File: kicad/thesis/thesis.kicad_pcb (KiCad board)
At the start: 2 copper layers, 100 x 75 mm, 22 parts, among them J1 Conn_01x01_Socket, J2 Conn_01x01_Socket, J3 Conn_01x07_Socket, J4 Conn_01x04_Socket, Q1 IRLZB8721, U1 INA219AxD

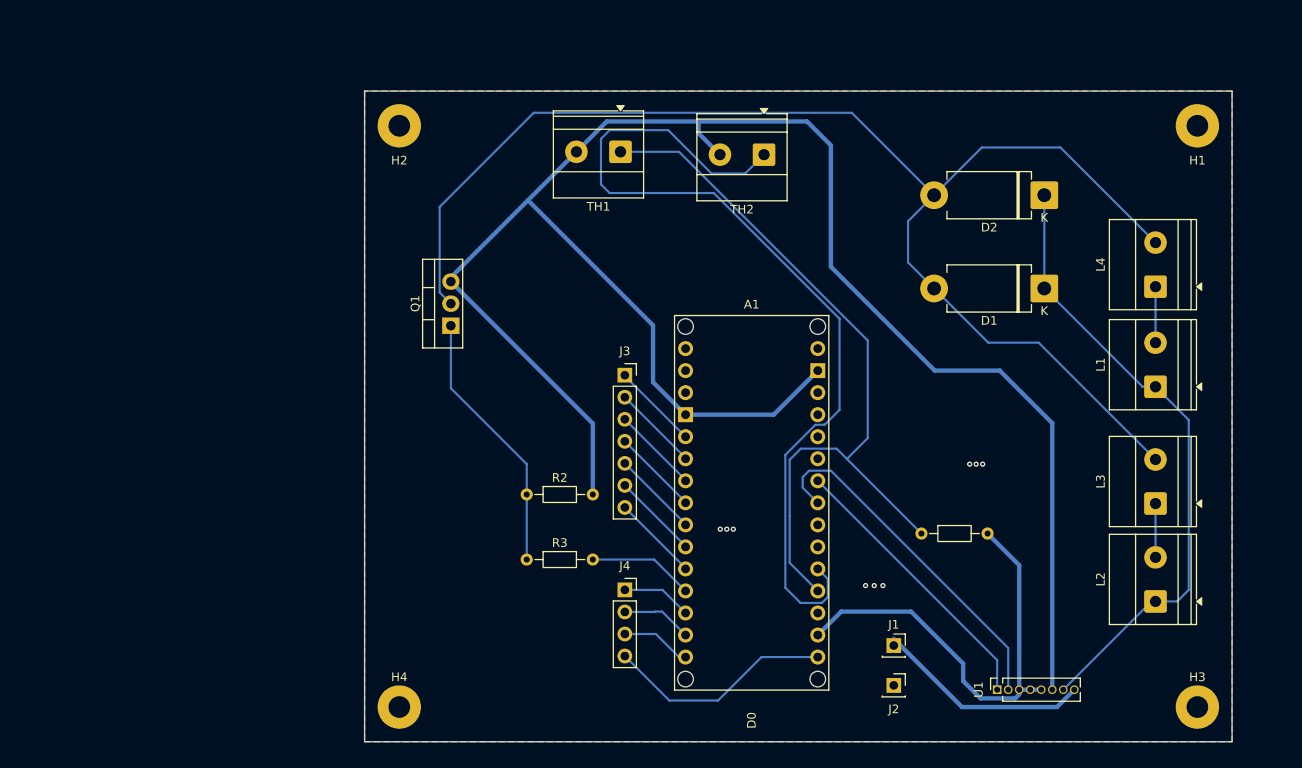
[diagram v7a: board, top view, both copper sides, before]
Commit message: Added pin sockets, header expansion, fixed INA and RC circuit
Need more labels but for now ok ra
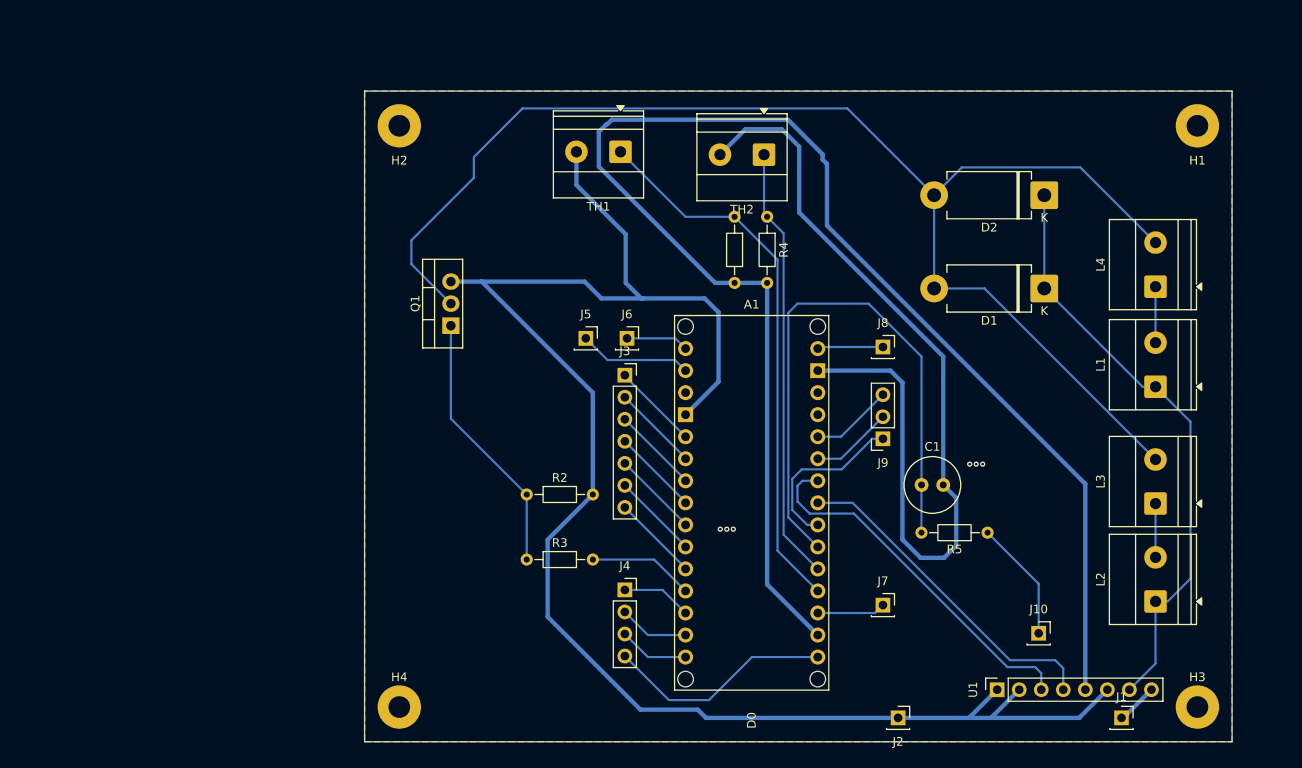
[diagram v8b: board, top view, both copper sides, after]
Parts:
- added C1: 100uF, Capacitor_THT:C_Radial_D6.3mm_H7.0mm_P2.50mm, F.Cu at (158.2, 104.4)
- added J10: Conn_01x01_Socket, Connector_PinSocket_2.54mm:PinSocket_1x01_P2.54mm_Vertical, F.Cu at (171.7, 121.5)
- added J5: Conn_01x01_Socket, Connector_PinSocket_2.54mm:PinSocket_1x01_P2.54mm_Vertical, F.Cu at (119.5, 87.5)
- added J6: Conn_01x01_Socket, Connector_PinSocket_2.54mm:PinSocket_1x01_P2.54mm_Vertical, F.Cu at (124.2, 87.5)
- added J7: Conn_01x01_Socket, Connector_PinSocket_2.54mm:PinSocket_1x01_P2.54mm_Vertical, F.Cu at (153.8, 118.2)
- added J8: Conn_01x01_Socket, Connector_PinSocket_2.54mm:PinSocket_1x01_P2.54mm_Vertical, F.Cu at (153.8, 88.5)
- added J9: Conn_01x03_Socket, Connector_PinSocket_2.54mm:PinSocket_1x03_P2.54mm_Vertical, F.Cu at (153.8, 99.1)
- added R4: 10K, Resistor_THT:R_Axial_DIN0204_L3.6mm_D1.6mm_P7.62mm_Horizontal, F.Cu at (140.4, 73.5)
- added R5: 500, Resistor_THT:R_Axial_DIN0204_L3.6mm_D1.6mm_P7.62mm_Horizontal, F.Cu at (165.8, 109.9)
- U1: footprint Connector_PinSocket_1.27mm:PinSocket_1x08_P1.27mm_Vertical -> Connector_PinSocket_2.54mm:PinSocket_1x08_P2.54mm_Vertical
- moved R1 42.4 mm to (136.7, 73.5), turned to -90 degrees
- moved J1 27.5 mm to (181.2, 131.2)
- moved J2 3.78 mm to (155.5, 131.2)
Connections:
- A1 pad A2: unconnected-(A1-PadA2) -> Net-(A1-PadA2)
- A1 pad A3: unconnected-(A1-PadA3) -> Net-(J9-Pin_1)
- A1 pad A6: unconnected-(A1-PadA6) -> Net-(J9-Pin_2)
- A1 pad A7: unconnected-(A1-PadA7) -> Net-(J9-Pin_3)
- A1 pad AREF: unconnected-(A1-PadAREF) -> Net-(J7-Pin_1)
- A1 pad D0: unconnected-(A1-D0/RX-PadD0) -> Net-(A1-D0/RX)
- A1 pad D1: unconnected-(A1-D1/TX-PadD1) -> Net-(A1-D1/TX)
- A1 pad VIN: unconnected-(A1-PadVIN) -> Net-(J8-Pin_1)
- U1 pad 1: /A1 -> GND
- U1 pad 2: /A0 -> GND
- U1 pad 3: +3.3V -> /A1
- U1 pad 4: +3.3V -> /A0
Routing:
- net +3.3V: track 52.4 -> 174.2 mm
- net GND: track 216.3 -> 292.6 mm, vias 9 -> 6
- net Net-(A1-PadA2): track 0.00 -> 67.0 mm
- net Net-(A1-PadA1): track 105.2 -> 50.3 mm
- net Net-(A1-PadA0): track 88.4 -> 63.4 mm
- net Vin: track 24.9 -> 4.80 mm
- net Net-(J9-Pin_1): track 0.00 -> 19.6 mm
- net Net-(J10-Pin_1): track 0.00 -> 14.0 mm
- net Net-(A1-D0/RX): track 0.00 -> 13.0 mm
- net /A1: track 32.6 -> 42.6 mm
- net Net-(J9-Pin_3): track 0.00 -> 9.51 mm
- net Net-(J9-Pin_2): track 0.00 -> 9.51 mm
- net Net-(J7-Pin_1): track 0.00 -> 7.89 mm
- net Net-(J8-Pin_1): track 0.00 -> 7.58 mm
- net Net-(A1-D1/TX): track 0.00 -> 7.24 mm
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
